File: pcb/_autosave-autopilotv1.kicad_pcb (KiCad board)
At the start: 2 copper layers, 111 x 78 mm, 17 parts, among them J1 Conn_01x01, SW1 My2pin_SW_MEC_5G, SW10 My2pin_SW_MEC_5G, SW11 Rotary_Encoder_Switch, SW12 Rotary_Encoder_Switch, SW13 Rotary_Encoder_Switch, SW14 Rotary_Encoder_Switch, SW15 Rotary_Encoder_Switch, SW2 My2pin_SW_MEC_5G, SW3 My2pin_SW_MEC_5G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

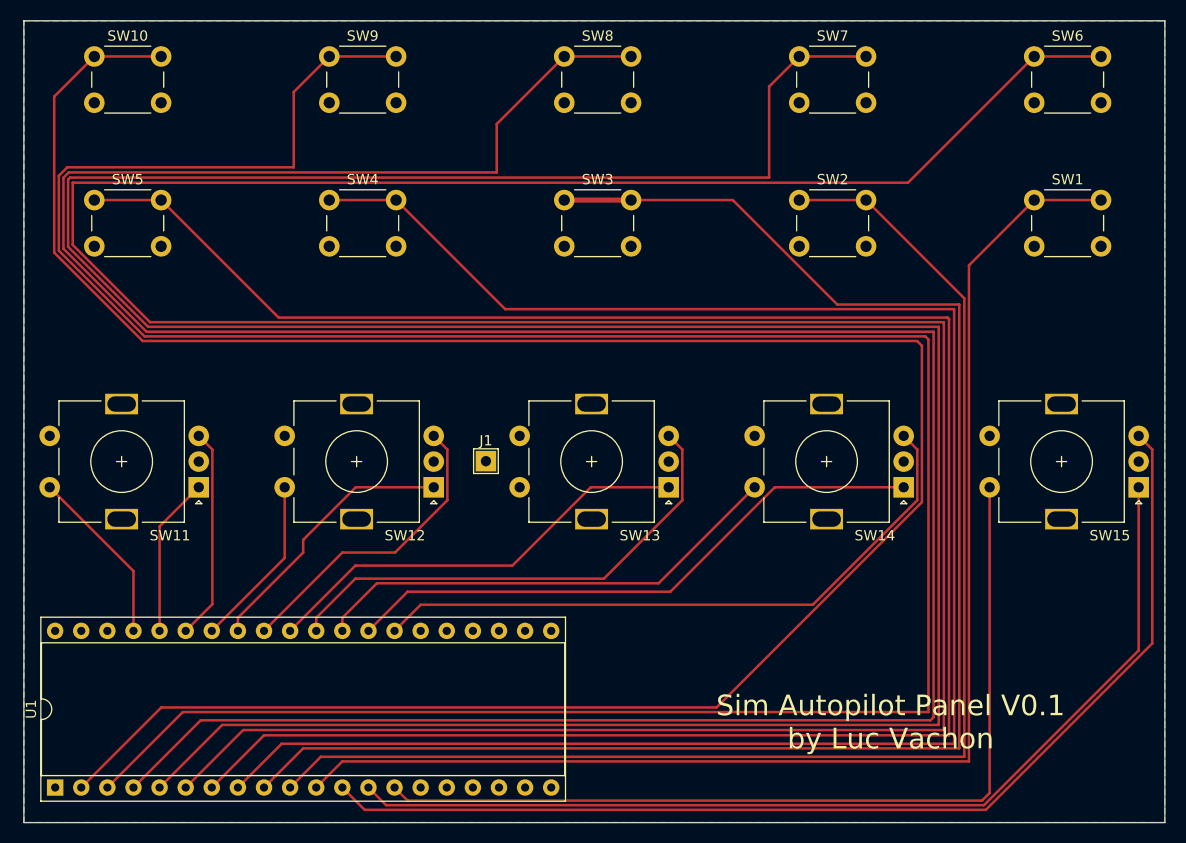
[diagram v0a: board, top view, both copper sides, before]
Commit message: more cleanup and some pics
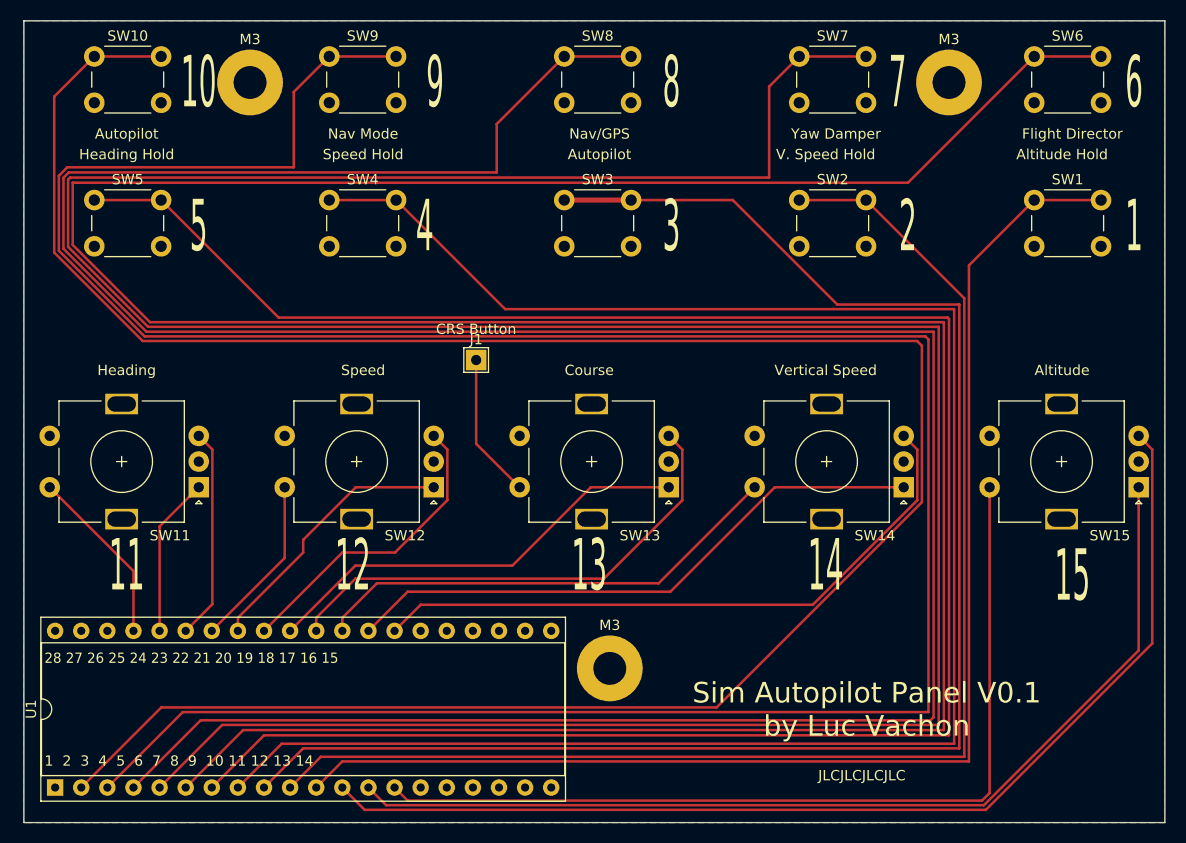
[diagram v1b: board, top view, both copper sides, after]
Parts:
- added M3: MountingHole_3.2mm_M3_Pad, MountingHole:MountingHole_3.2mm_M3_Pad, F.Cu at (120.0, 137.0)
- added M3: MountingHole_3.2mm_M3_Pad, MountingHole:MountingHole_3.2mm_M3_Pad, F.Cu at (85.0, 80.0)
- added M3: MountingHole_3.2mm_M3_Pad, MountingHole:MountingHole_3.2mm_M3_Pad, F.Cu at (153.0, 80.0)
- moved J1 9.89 mm to (107.0, 107.0)
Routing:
- net Net-(J1-Pad1): track 0.00 -> 14.1 mm
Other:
- board text added: "1"
- board text added: "1 2 3 4 5 6 7 8 9 10 11 12 13 14"
- board text added: "10"
- board text added: "11"
- board text added: "12"
- board text added: "13"
- board text added: "14"
- board text added: "15"
- board text added: "2"
- board text added: "28 27 26 25 24 23 22 21 20 19 18 17 16 15"
- board text added: "3"
- board text added: "4"
- board text added: "5"
- board text added: "6"
- board text added: "7"
- board text added: "8"
- board text added: "9"
- board text added: "Altitude"
- board text added: "Altitude Hold"
- board text added: "Autopilot"
- board text added: "CRS Button"
- board text added: "Course"
- board text added: "Flight Director"
- board text added: "Heading"
- board text added: "Heading Hold"
- board text added: "JLCJLCJLCJLC"
- board text added: "Nav Mode"
- board text added: "Nav/GPS"
- board text added: "Speed"
- board text added: "Speed Hold"
- board text added: "V. Speed Hold"
- board text added: "Vertical Speed"
- board text added: "Yaw Damper"
